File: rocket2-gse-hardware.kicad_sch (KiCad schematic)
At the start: 47 parts, among them J1 ARMING_PLUG, J1 USB_C Connector, J8 Conn_01x02_Pin, Q2 n-MOSFET, Y1 16MHz

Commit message: fix
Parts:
- J1: Manufacturer Generic -> (none); Part # Generic 2x5.08 Screw Terminal -> (none)
- J8: value Conn_01x02_Pin -> PWR; Manufacturer Generic -> (none); Part # Generic 2x5.08 Screw Terminal -> (none)
- J8: value Conn_01x02_Pin -> ALARM; Manufacturer Generic -> (none); Part # Generic 2x5.08 Screw Terminal -> (none)
- Q2: value n-MOSFET -> ~; symbol UCIRP-KiCAD-Lib:Q_NMOS_GDS -> Device:Q_NMOS_GSD
- R1: value 1K -> 68K; Part # Generic 1K 0402 Resistor -> Generic 68K 1% 0402 Resistor
- R13, R28, R54: Part # Generic 10K 0402 Resistor -> Generic 10K 1% 0402 Resistor
- R13, R14: Part # Generic 5K1 0402 Resistor -> Generic 5K1 1% 0402 Resistor
- R13: Part # Generic 100 0402 Resistor -> Generic 100 1% 0402 Resistor
- R2: value 3K3 -> 10K; Part # Generic 3K3 0402 Resistor -> Generic 10K 1% 0402 Resistor
- R28, R29: Part # Generic 100K 0402 Resistor -> Generic 100K 1% 0402 Resistor
- R30: value 220 -> 470; Part # Generic 220 0402 Resistor -> Generic 470 1% 0402 Resistor
- R31: value 470 -> 1K; Part # Generic 470 0402 Resistor -> Generic 1K 1% 0402 Resistor
- R32: value 2K -> 3.3K; Part # Generic 2K 0402 Resistor -> Generic 3.3K 1% 0402 Resistor
- R33: Part # Generic 470 0402 Resistor -> Generic 470 1% 0402 Resistor
- R53: value 70K -> 68K; Part # Generic 70K 0402 Resistor -> Generic 68K 1% 0402 Resistor
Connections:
- net +24V: now also J8.1 (Pin_1); no longer Q2.2 (D)
- net GND: now also Q2.2 (S); no longer J8.2 (Pin_2)
- net at Q2.3 (D): now also J8.2 (Pin_2); no longer J8.1 (Pin_1)
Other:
- moved on the sheet: J8, Q2, R13

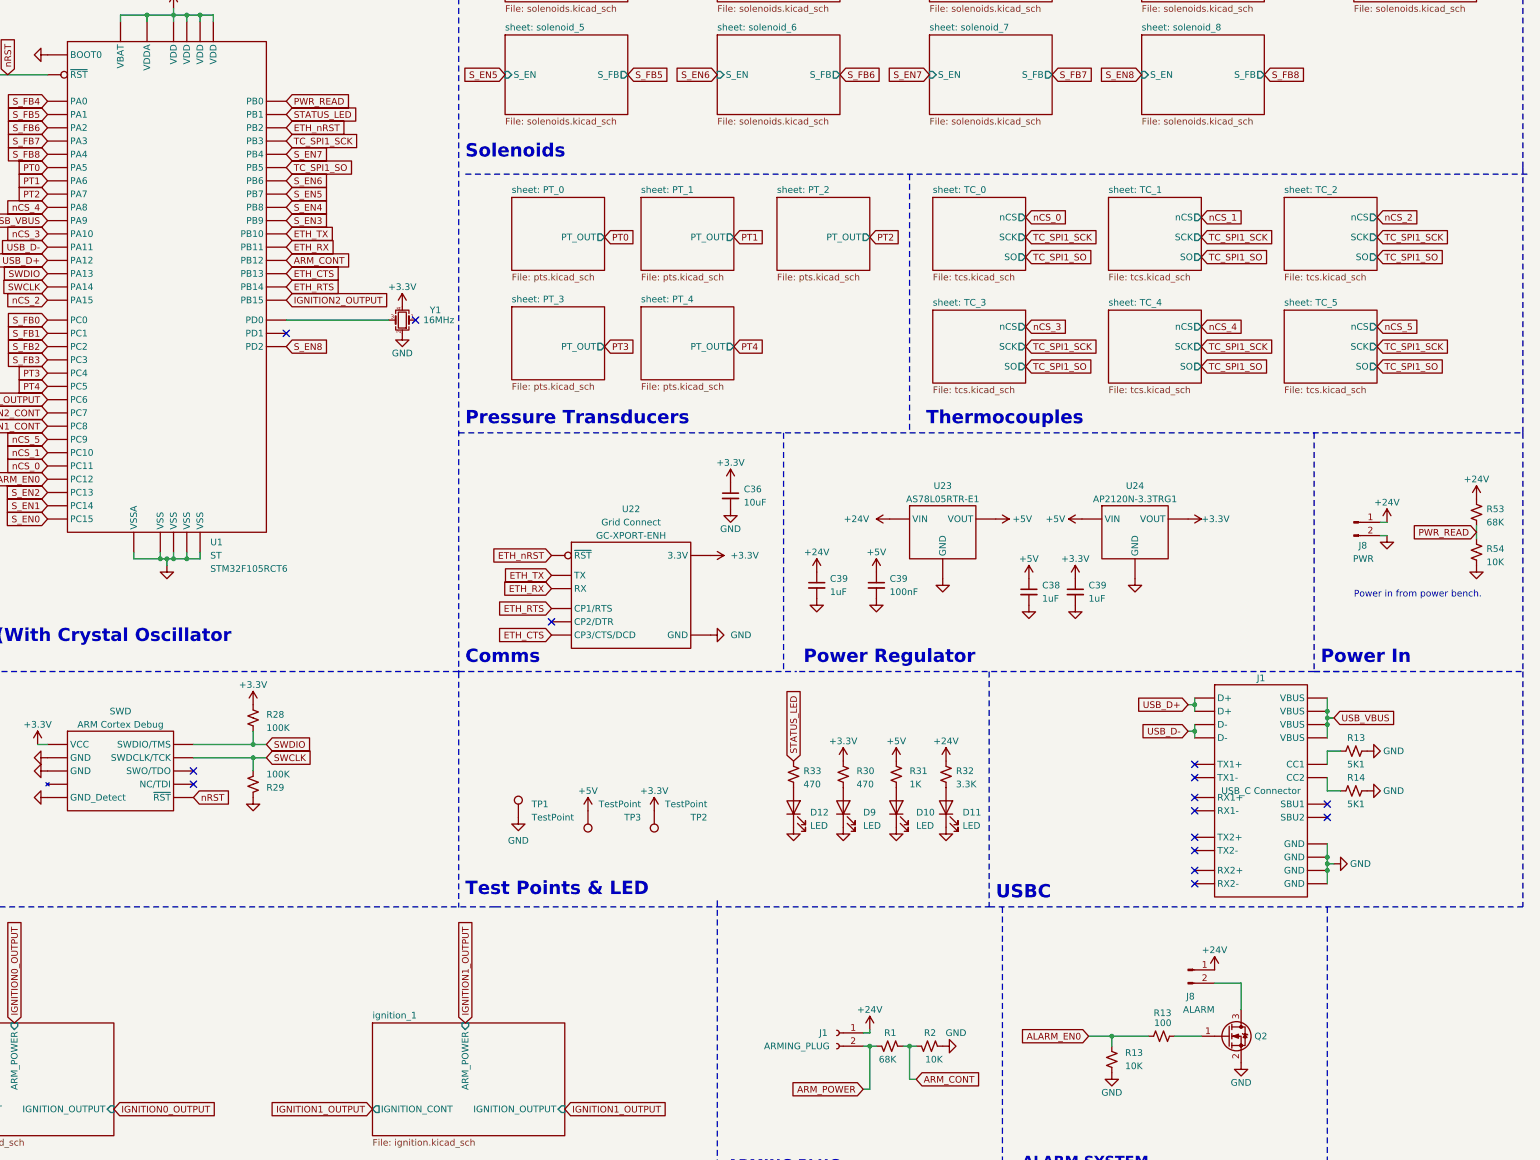
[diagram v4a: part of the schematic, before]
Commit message: Added in dual power, fuse, status led, and comments
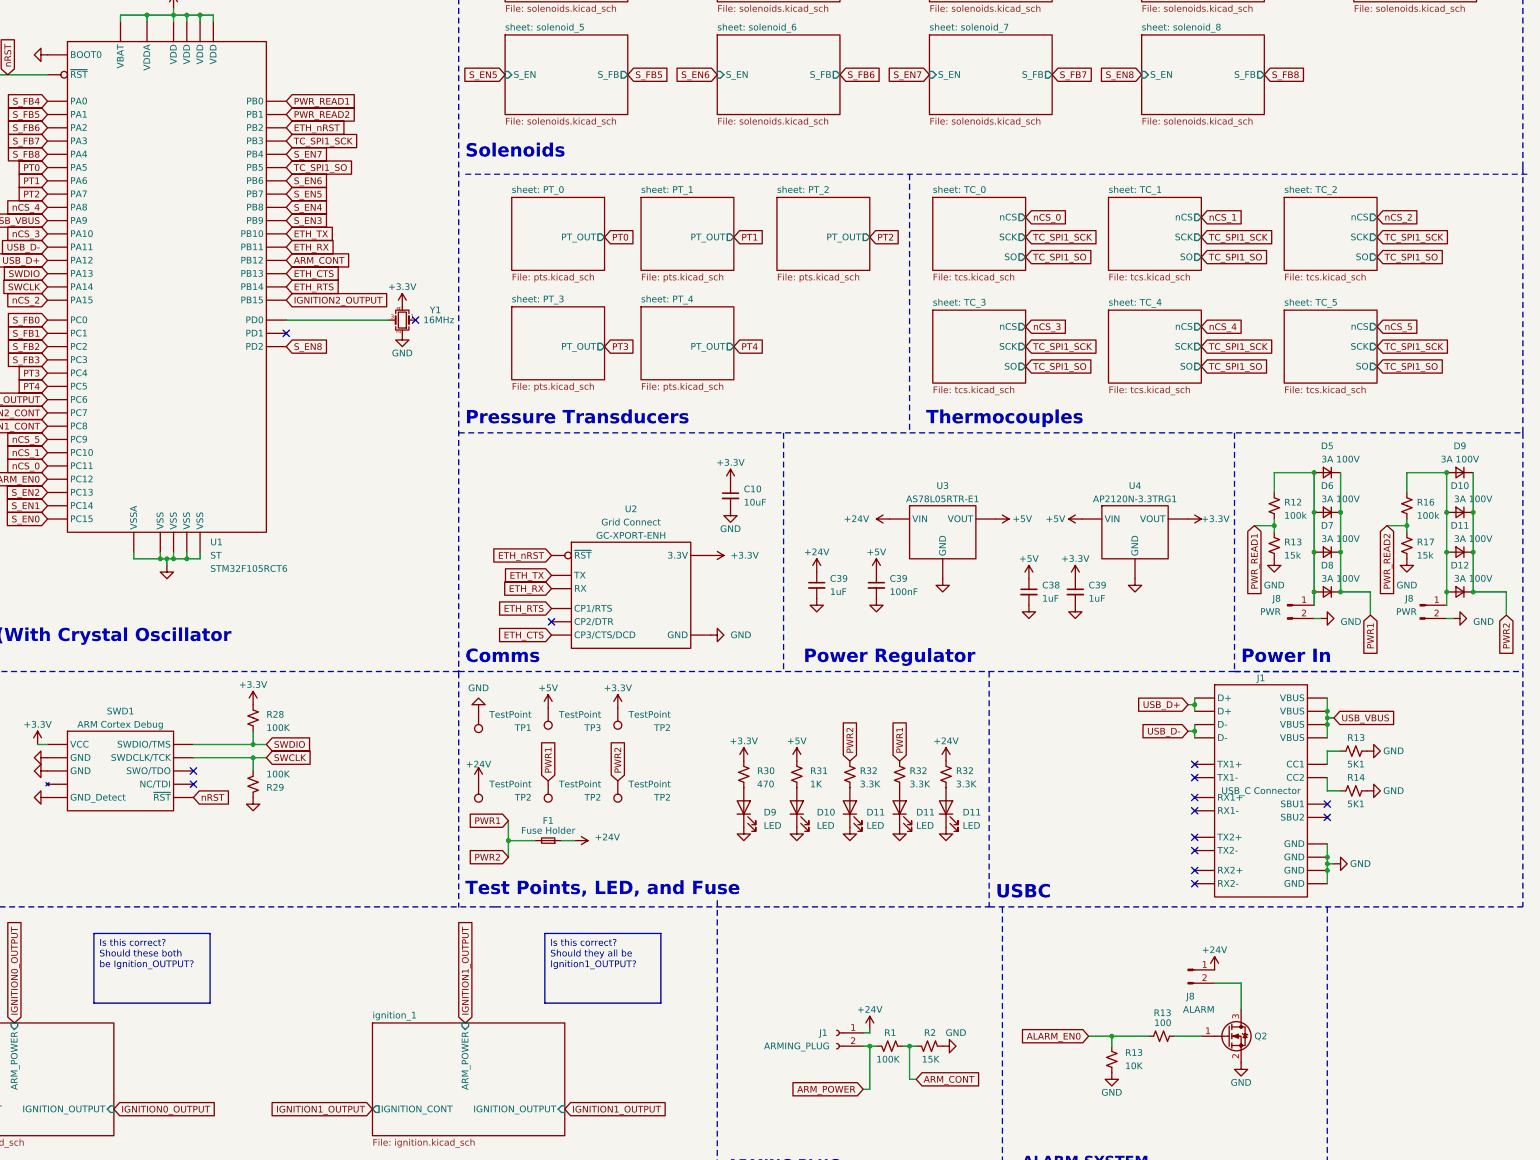
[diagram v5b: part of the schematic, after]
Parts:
- removed D12: LED, LED_SMD:LED_0603_1608Metric, symbol UCIRP-KiCAD-Lib:LED
- removed R33: 470, Resistor_SMD:R_0402_1005Metric, symbol UCIRP-KiCAD-Lib:R_Small_US
- added D10, D11, D12, D5, D6, D7, D8, D9: 3A 100V, symbol Device:D_Small
- added D11 (x2): LED, LED_SMD:LED_0603_1608Metric, symbol UCIRP-KiCAD-Lib:LED
- added F1: Fuse Holder, symbol Device:Fuse_Small
- added J8: PWR, TerminalBlock:TerminalBlock_bornier-2_P5.08mm, symbol UCIRP-KiCAD-Lib:Conn_01x02_Pin
- added R16: 100k, Resistor_SMD:R_0402_1005Metric, symbol UCIRP-KiCAD-Lib:R_Small_US
- added R17: 15k, Resistor_SMD:R_0402_1005Metric, symbol UCIRP-KiCAD-Lib:R_Small_US
- added R32 (x2): 3.3K, Resistor_SMD:R_0402_1005Metric, symbol UCIRP-KiCAD-Lib:R_Small_US
- added TP2 (x3): TestPoint, TestPoint:TestPoint_Pad_D2.0mm, symbol UCIRP-KiCAD-Lib:TestPoint
- R1: value 68K -> 100K
- R12: renamed from R53; value 68K -> 100k
- R13: renamed from R54; value 10K -> 15k
- R2: value 10K -> 15K
- renumbered C36 to C10, SWD to SWD1, U22 to U2, U23 to U3, U24 to U4
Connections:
- net +24V: now also F1.1, TP2.1; no longer J8.1 (Pin_1), R12.1
- net GND: now also D11.1 (K), D11.1 (K), J8.2 (Pin_2), R17.2
- net PWR_READ renamed PWR_READ1
- net STATUS_LED renamed PWR_READ2
- net PWR_READ2: now also R16.2, R17.1
- new net: D10.2 (A), D11.2 (A), D12.2 (A), D9.2 (A), J8.1 (Pin_1), R16.1
- new net: D11.2 (A), R32.1 (x2)
- new net: D5.2 (A), D6.2 (A), D7.2 (A), D8.2 (A), J8.1 (Pin_1), R12.1
- new net PWR1: D10.1 (K), D11.1 (K), D12.1 (K), D5.1 (K), D6.1 (K), D7.1 (K), D8.1 (K), D9.1 (K), F1.2, R32.2, R32.2, TP2.1, TP2.1
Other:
- note added: "Test Points, LED, and Fuse"
- note removed: "Power in from power bench."
- note removed: "Test Points & LED"
- moved on the sheet: D10, D9, J8, R12, R13, R30, R31, TP1, TP2, TP3
